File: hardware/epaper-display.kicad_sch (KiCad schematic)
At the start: 72 parts, among them J1 AES200200A00 FPC, J2 USB-C 2.0 receptacle, J3 LiPo cell (B+/B-), J4 I2C temp (optional), J5 UART, J6 GPIO expansion, Q1 Si1304BDL / NX3008NBK, Q2 FS8205A, SW1 EN/RESET, SW2 BOOT, SW3 BTN_UP, SW4 BTN_DOWN, SW5 BTN_LEFT, SW6 BTN_RIGHT, SW7 BTN_SELECT, SW8 BTN_CANCEL, U1 ESP32-S3-WROOM-1-N8, U2 MCP73831T-2ACI/OT, U3 TLV75733PDBVR, U4 DW01A

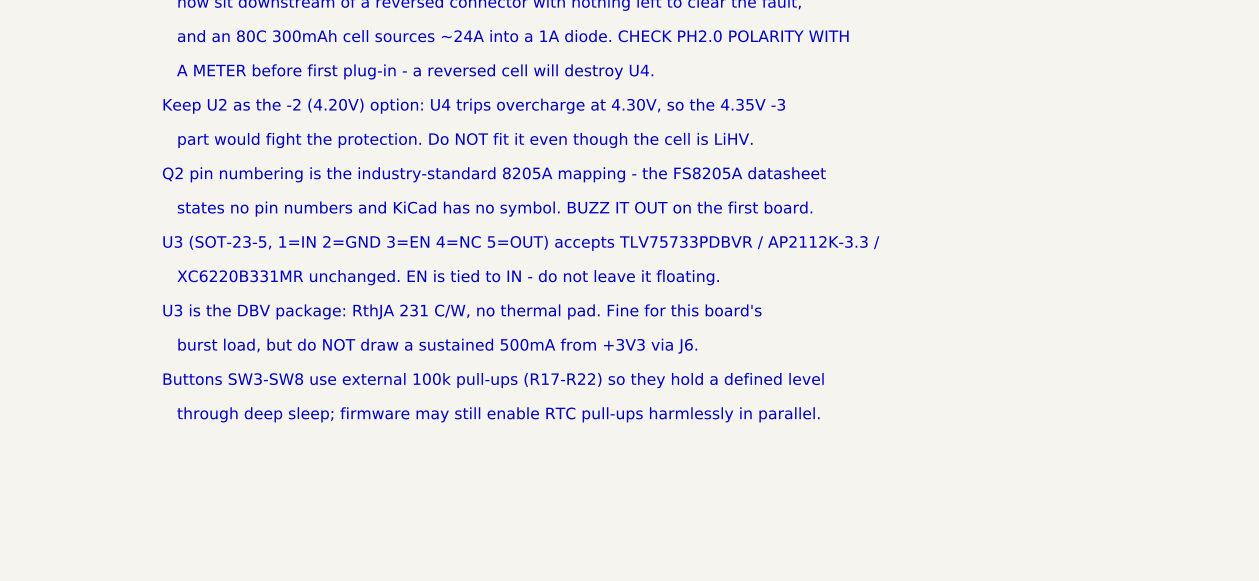
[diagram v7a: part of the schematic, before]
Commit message: hardware: FS8205A pinout is unresolved, not confirmed — flag it hard
The Tech Public FS8205A datasheet does not confirm the pin numbering.
It contradicts it, which makes the open item sharper rather than
closing it.

What it adds: a "Package and Pin Configuration" isometric that labels
functions by position -- one row S1 / D1/D2 / S2, the other row G1 /
D1/D2 / G2. Sources at the ends of one row, gates at the ends of the
other, a drain in the MIDDLE of each row.

That arrangement is incompatible with the commonly-quoted 8205A mapping
currently wired (1=S1 2=G1 3=S2 4=G2 5=D2 6=D1), which puts a gate in
the middle of the source row and both drains adjacent on the other. The
two candidates agree on pins 1, 3, 4, 5 and differ on 2 and 6:

  (A) as wired now:  1=S1 2=G1 3=S2 4=G2 5=D2 6=D1
  (B) Tech Public:   1=S1 2=D   3=S2 4=G2 5=D  6=G1

Under (B) the current wiring drives PROT_DO into a drain and ties G1 to
the drain node -- the protection would silently not work.

Deliberately NOT switching to (B). Reading pin numbers off an isometric
means inferring pin 1 from a moulded dot, so (B) would trade one
unverified mapping for another. Neither datasheet in components/ has a
pin-number table and KiCad has no FS8205A symbol, so there is no third
source to break the tie.

Instead the flag is escalated everywhere it can be seen -- symbol
comment, BOM line, README 4, assembly notes and the schematic sheet --
with both candidates tabulated and a DMM procedure that settles it in
about a minute: the shorted pair are the drains; diode-mode ~0.6 V to
the drain node identifies the two sources; the remaining two are gates,
paired with the source at their own end.

Everything else in this design is confirmed against a datasheet. This is
the one open item, and it must be measured before a PCB is ordered.

Adds fs8205a-techpublic.pdf to components/.

Co-Authored-By: Claude Opus 5 <noreply@anthropic.com>
Claude-Session: https://claude.ai/code/session_017ASByNz7rVoZ3Zy31jhNCB
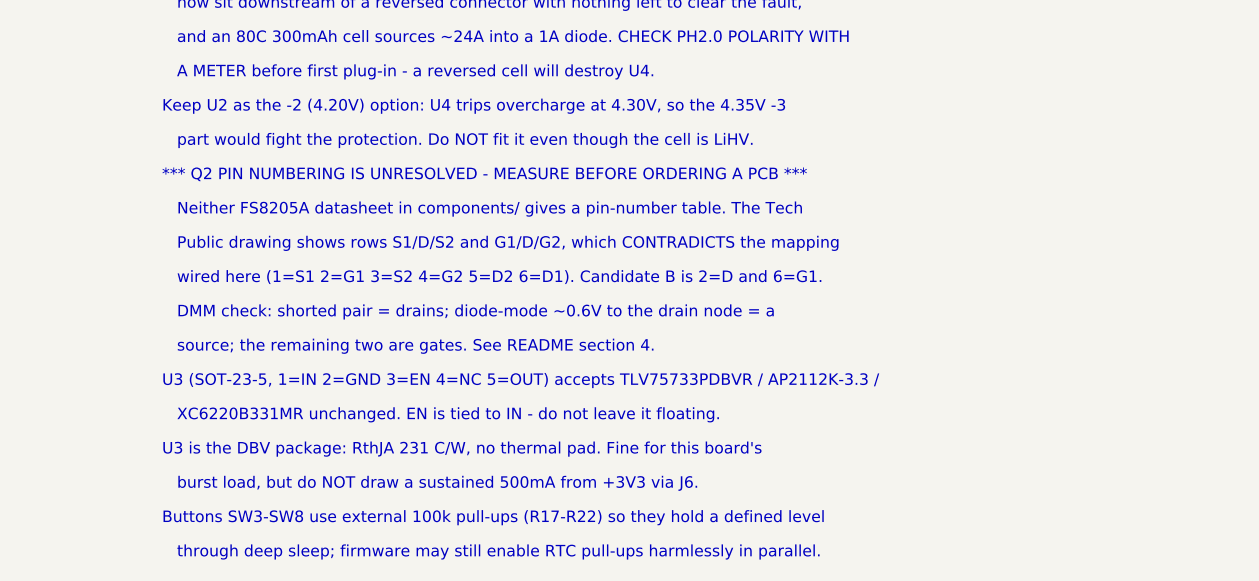
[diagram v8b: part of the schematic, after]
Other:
- note added: "*** Q2 PIN NUMBERING IS UNRESOLVED - MEASURE BEFORE ORDERING A PCB ***"
- note added: "DMM check: shorted pair = drains; diode-mode ~0.6V to the drain node = a"
- note added: "Neither FS8205A datasheet in components/ gives a pin-number table. The Tech"
- note added: "Public drawing shows rows S1/D/S2 and G1/D/G2, which CONTRADICTS the mapping"
- note added: "source; the remaining two are gates. See README section 4."
- note added: "wired here (1=S1 2=G1 3=S2 4=G2 5=D2 6=D1). Candidate B is 2=D and 6=G1."
- note removed: "Q2 pin numbering is the industry-standard 8205A mapping - the FS8205A datasheet"
- note removed: "states no pin numbers and KiCad has no symbol. BUZZ IT OUT on the first board."
